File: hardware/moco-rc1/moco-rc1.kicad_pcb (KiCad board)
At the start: 4 copper layers, 35 x 35 mm, 89 parts, among them J1 OUT_U, J2 OUT_V, J3 OUT_W, J4 Conn_02x03_Odd_Even, J5 VM+, J6 VM-, J7 CAN, Q1 FDMD8240LET40, Q2 FDMD8240LET40, Q3 FDMD8240LET40, SW1 RESET, U1 STSPIN32F0A, U2 TCAN4550, U3 AS5600, Y1 40MHz

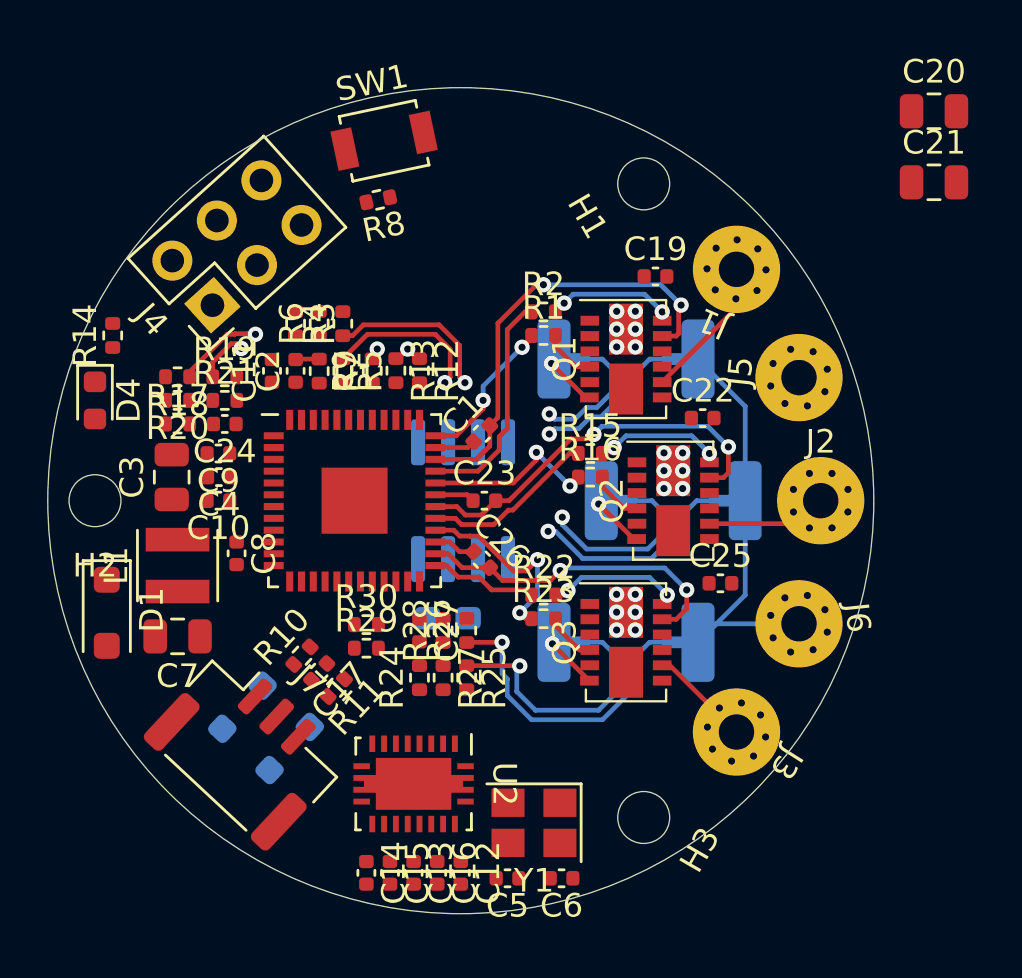
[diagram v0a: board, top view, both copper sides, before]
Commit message: Fix SVPWM (fabs())
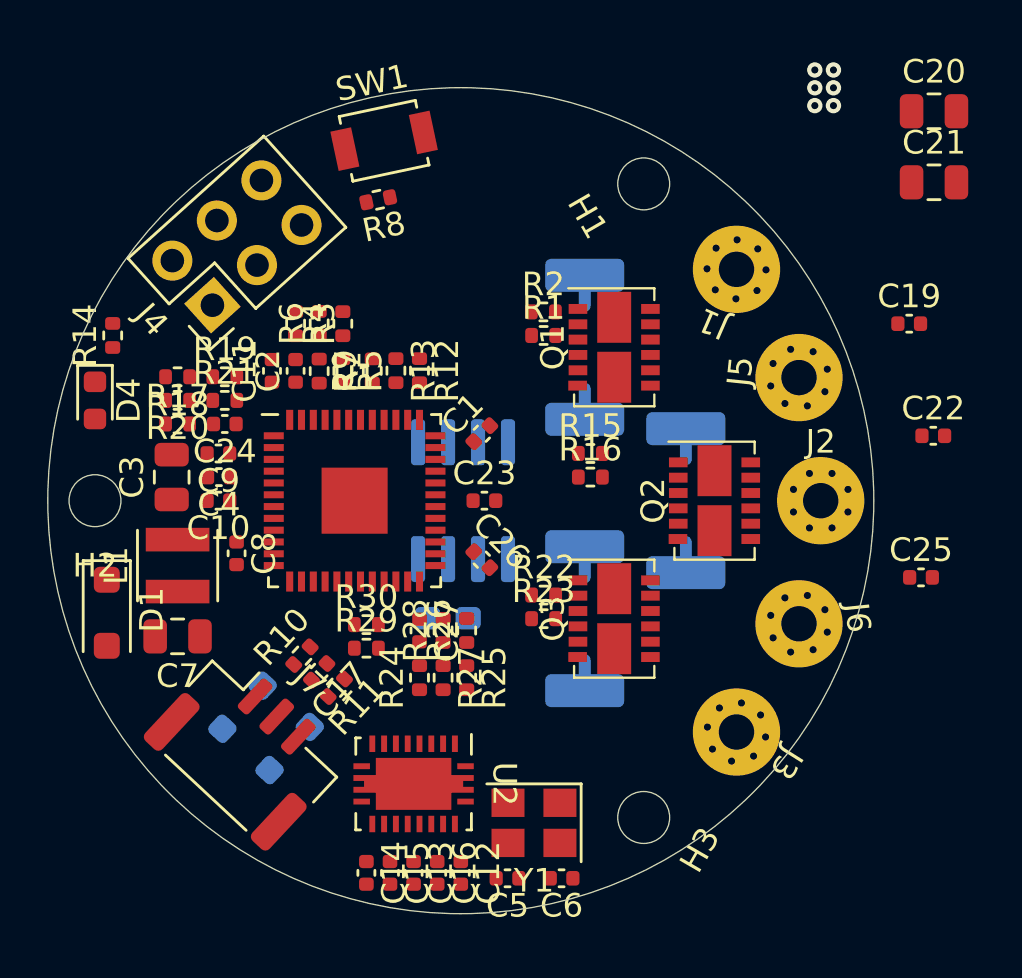
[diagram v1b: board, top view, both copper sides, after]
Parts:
- moved C19 10.9 mm to (169.0, 92.5)
- moved C22 9.80 mm to (170.0, 97.2)
- moved C25 8.50 mm to (169.5, 103.2)
- moved NT6 5.15 mm to (155.2, 102.8), turned to -90 degrees
- moved NT2 4.85 mm to (155.2, 91.2), turned to -90 degrees
- moved NT3 3.58 mm to (159.5, 102.2), turned to 90 degrees
- moved NT4 2.83 mm to (159.5, 97.8), turned to -90 degrees
- moved RS3 2.02 mm to (155.2, 105.0), turned to 90 degrees
- moved NT1 1.82 mm to (155.2, 95.8), turned to 90 degrees
- moved RS1 1.82 mm to (155.2, 93.5), turned to 90 degrees
- moved Q2 1.75 mm to (160.8, 100.0)
- moved NT5 1.35 mm to (155.2, 107.2), turned to 90 degrees
- moved Q3 1.12 mm to (156.5, 105.0)
- moved Q1 0.71 mm to (156.5, 93.5)
- moved RS2 0.53 mm to (159.5, 100.0), turned to 90 degrees
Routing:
- net /Power Stage/RS_U-: track 24.1 -> 0.00 mm, vias 2 -> 0
- net /Power Stage/RS_U+: track 23.9 -> 0.00 mm, vias 2 -> 0
- net /Power Stage/RS_V-: track 23.7 -> 0.00 mm, vias 2 -> 0
- net /Power Stage/RS_V+: track 22.9 -> 0.00 mm, vias 2 -> 0
- net GND: track 18.8 -> 0.00 mm, vias 1 -> 0
- net /Power Stage/QO_U: track 18.7 -> 0.00 mm, vias 2 -> 0
- net /Power Stage/QO_V: track 16.5 -> 0.00 mm, vias 2 -> 0
- net /Power Stage/QO_W: track 13.7 -> 0.00 mm, vias 2 -> 0
- net /Power Stage/RS_W-: track 13.2 -> 0.00 mm, vias 1 -> 0
- net /Power Stage/RS_W+: track 11.5 -> 0.00 mm, vias 1 -> 0
- net Net-(U1D-HSU): track 9.82 -> 0.00 mm
- net Net-(U1B-LSW): track 8.41 -> 0.00 mm, vias 2 -> 0
- net Net-(U1C-LSV): track 7.53 -> 0.00 mm, vias 2 -> 0
- net Net-(U1C-HSV): track 7.41 -> 0.00 mm
- net Net-(U1D-LSU): track 6.45 -> 0.00 mm, vias 2 -> 0
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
